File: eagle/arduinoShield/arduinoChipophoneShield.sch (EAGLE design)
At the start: 17 parts

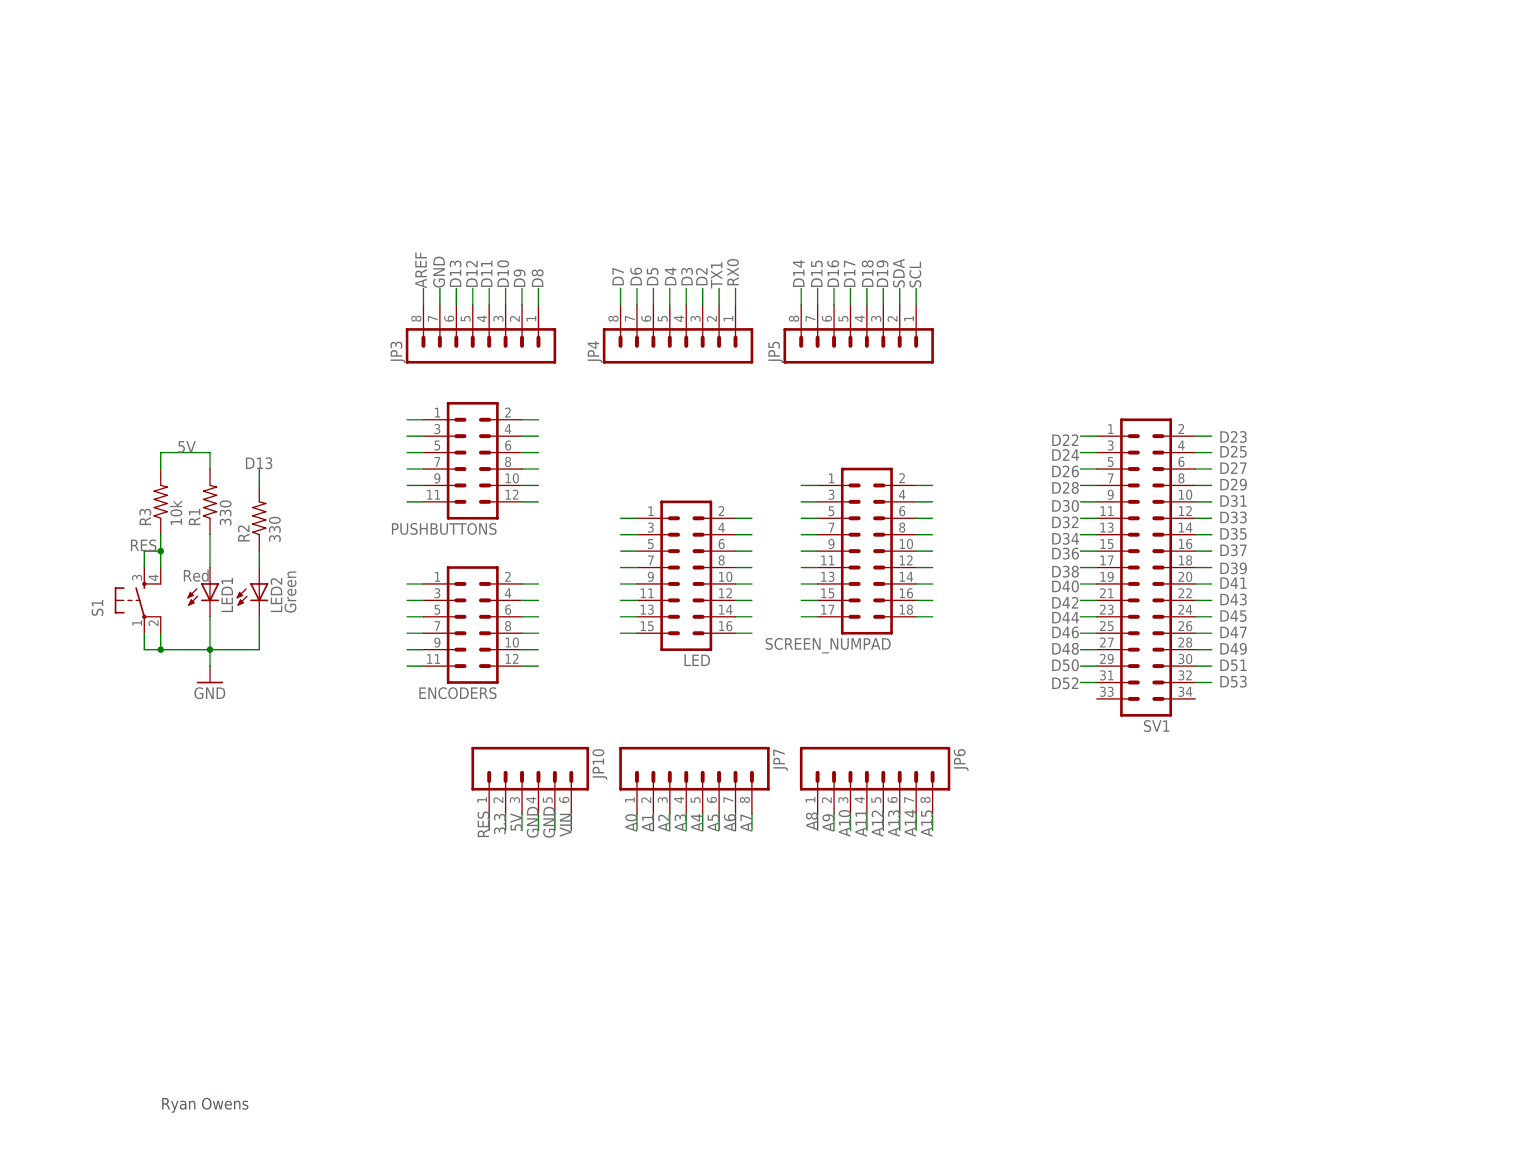
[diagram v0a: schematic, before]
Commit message: Added MIDI I/O, took out status light
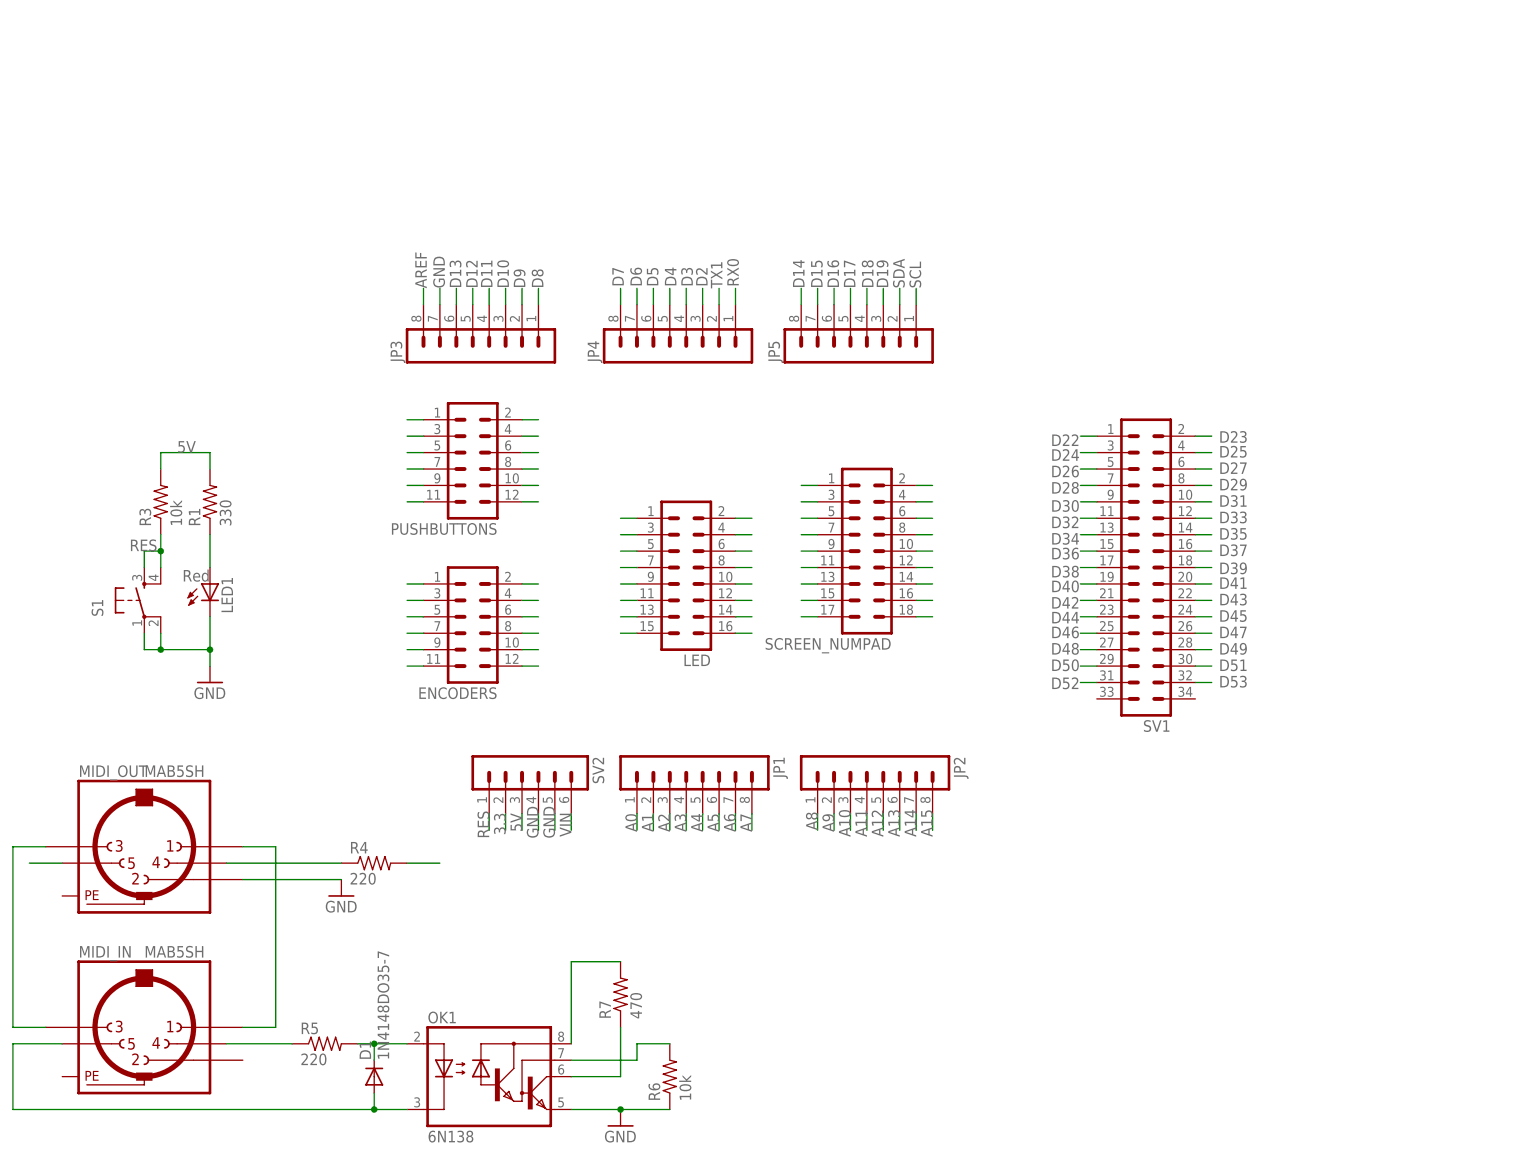
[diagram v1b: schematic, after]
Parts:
- removed JP10: (no value), SparkFun:M06LOCK
- removed JP6, JP7: (no value), SparkFun:M08LOCK
- removed LED2: Green, SparkFun:LED5MM
- removed R2: 330, SparkFun:RESISTORPTH1
- added D1: 1N4148DO35-7, diode:1N4148DO35-7
- added JP1, JP2: (no value), con-lstb:MA08-1
- added MIDI_IN, MIDI_OUT: MAB5SH, con-hirschmann:MAB5SH
- added OK1: 6N138, optocoupler:6N138
- added R4, R5: 220, rcl:R-US_0204/7
- added R6: 10k, rcl:R-US_0204/7
- added R7: 470, rcl:R-US_0204/7
- added SV2: (no value), con-lstb:MA06-1
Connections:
- removed net N$127: LED2.A, R2.1
- new net N$1: MIDI_IN.3, MIDI_OUT.3
- new net N$2: MIDI_IN.1, MIDI_OUT.1
- new net N$3: MIDI_OUT.4, R4.1
- new net N$5: D1.C, OK1.A, R5.2
- new net N$6: MIDI_IN.4, R5.1
- new net N$7: D1.A, MIDI_IN.5, OK1.C
- new net N$8: OK1.VB, R6.2
- net 3.3: now also SV2.2; no longer JP10.2
- net 5V: now also OK1.VCC, R4.2, R7.2, SV2.3; no longer JP10.3
- net A0: now also JP1.1; no longer JP7.1
- net A1: now also JP1.2; no longer JP7.2
- net A10: now also JP2.3; no longer JP6.3
- net A11: now also JP2.4; no longer JP6.4
- net A12: now also JP2.5; no longer JP6.5
- net A13: now also JP2.6; no longer JP6.6
- net A14: now also JP2.7; no longer JP6.7
- net A15: now also JP2.8; no longer JP6.8
- net A2: now also JP1.3; no longer JP7.3
- net A3: now also JP1.4; no longer JP7.4
- net A4: now also JP1.5; no longer JP7.5
- net A5: now also JP1.6; no longer JP7.6
- net A6: now also JP1.7; no longer JP7.7
- net A7: now also JP1.8; no longer JP7.8
- net A8: now also JP2.1; no longer JP6.1
- net A9: now also JP2.2; no longer JP6.2
- net D13: no longer R2.2
- net GND: now also MIDI_OUT.2, OK1.GND, R6.1, SV2.4, SV2.5; no longer JP10.4, JP10.5, LED2.C
- net RES: now also SV2.1; no longer JP10.1
- net RX0: now also OK1.VO, R7.1
- net TX1: now also MIDI_OUT.5
- net VIN: now also SV2.6; no longer JP10.6
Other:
- note removed: "Ryan Owens"

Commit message: Added ground/power plane as well as 5V DIN forwarding switches on Arduino Board
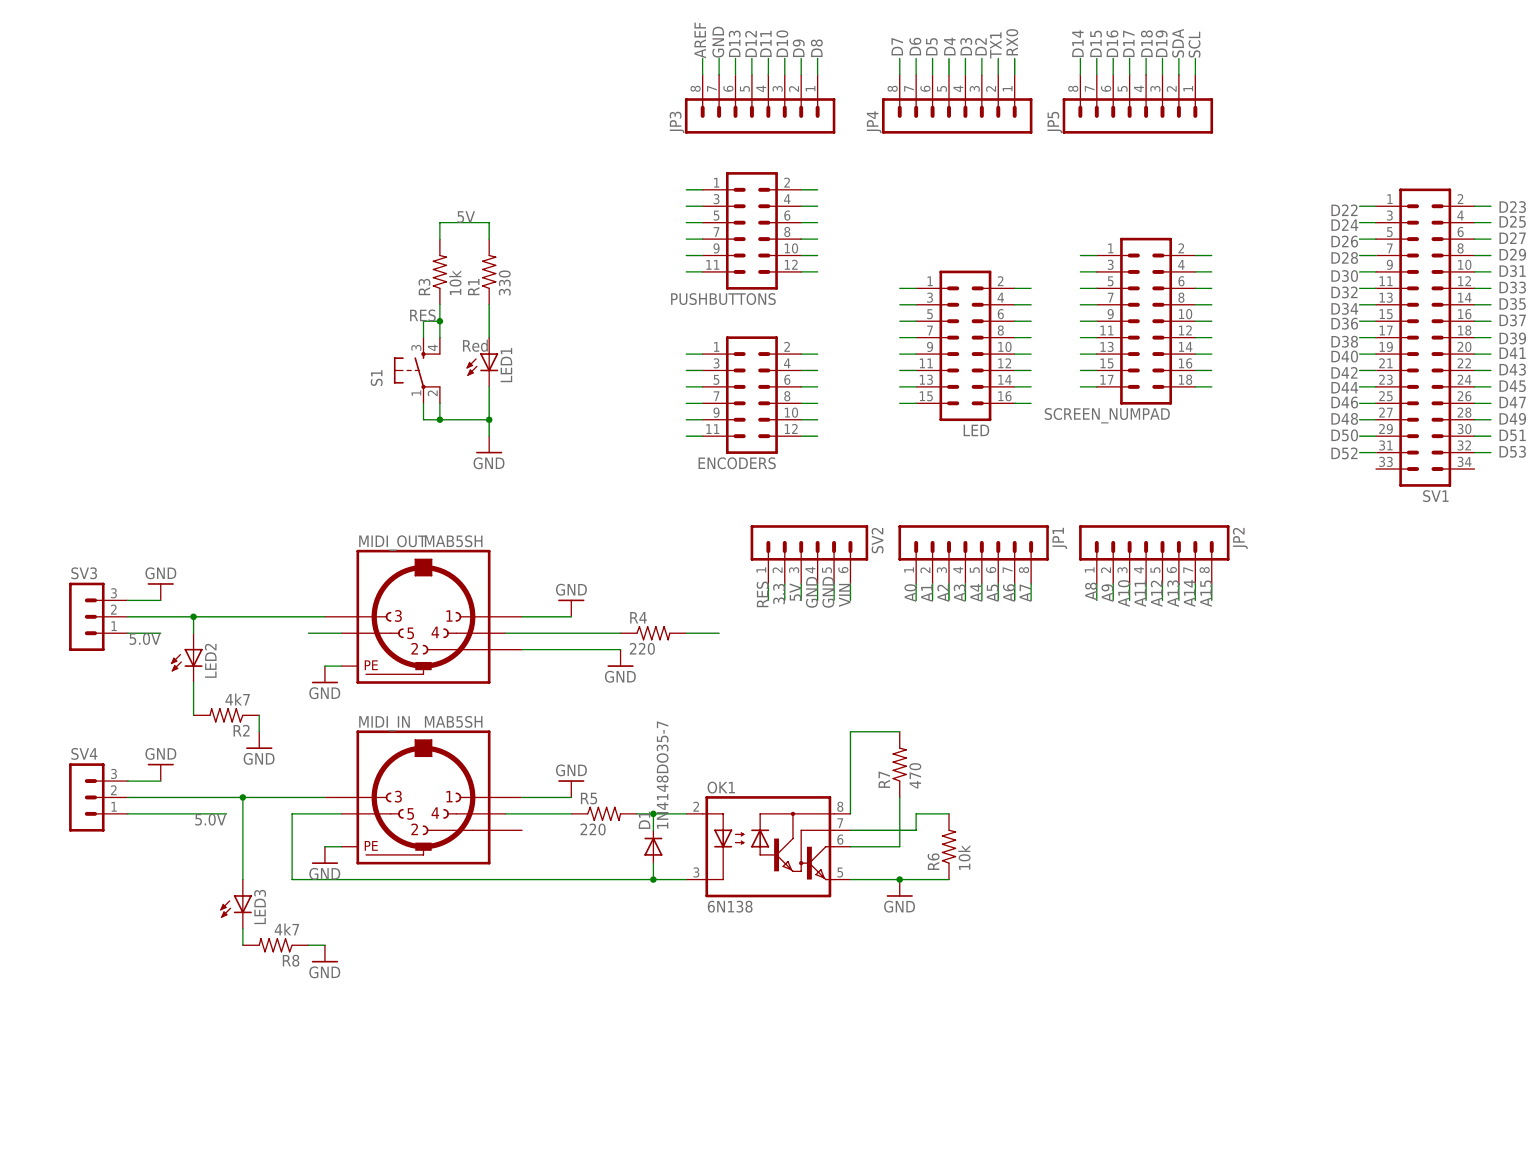
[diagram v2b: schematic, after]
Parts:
- added LED2, LED3: (no value), led:LEDLSU260
- added R2, R8: 4k7, resistor:R-US_0204/7
- added SV3, SV4: (no value), con-lstb:MA03-1
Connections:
- new net N$13: LED3.C, R8.2
- new net N$4: LED2.C, R2.2
- net 5V: now also SV3.1, SV4.1
- net GND: now also MIDI_IN.1, MIDI_IN.PE, MIDI_OUT.1, MIDI_OUT.PE, R2.1, R8.1, SV3.3, SV4.3
- net N$1: now also LED3.A, SV4.2; no longer MIDI_OUT.3
- net N$2: now also LED2.A, MIDI_OUT.3, SV3.2; no longer MIDI_IN.1, MIDI_OUT.1
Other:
- moved on the sheet: D1, ENCODERS, JP1, JP2, JP3, JP4, JP5, LED, LED1, MIDI_IN, MIDI_OUT, OK1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

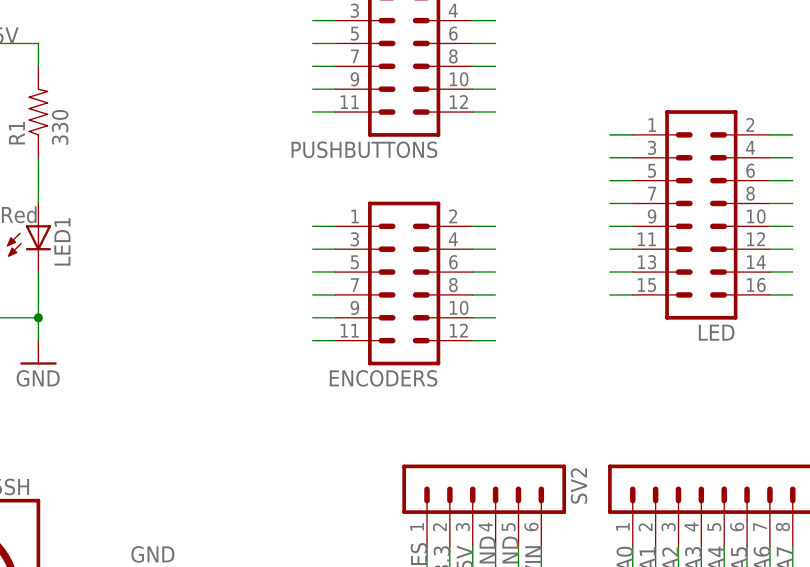
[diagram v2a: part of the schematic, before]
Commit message: Ripped up unnecessary traces due to ground/power planes. Also switched encoder common to ground to use internal pullup resistors
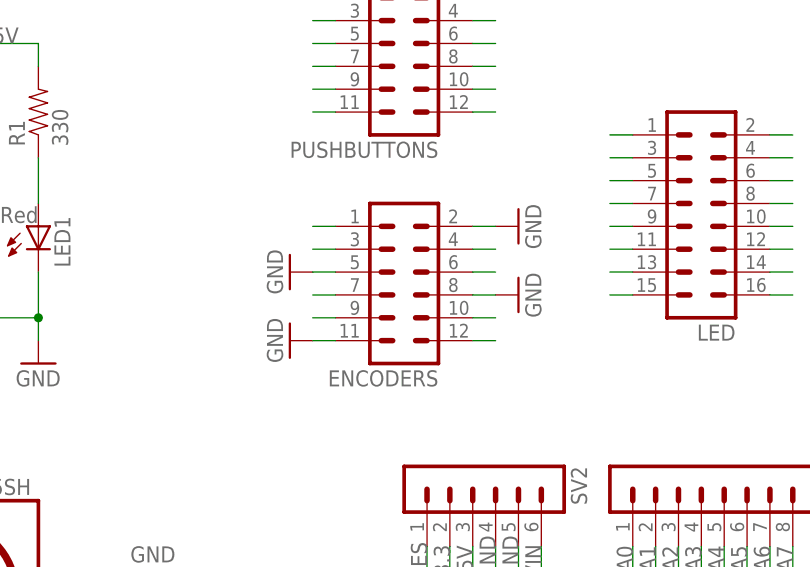
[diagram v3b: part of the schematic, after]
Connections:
- net 5V: no longer ENCODERS.11, ENCODERS.2, ENCODERS.5, ENCODERS.8
- net GND: now also ENCODERS.11, ENCODERS.2, ENCODERS.5, ENCODERS.8
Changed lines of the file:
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@@
 <part name="R8" library="resistor" deviceset="R-US_" device="0204/7" value="4k7"/>
 <part name="GND12" library="supply1" deviceset="GND" device=""/>
+<part name="GND9" library="SparkFun" deviceset="GND" device=""/>
+<part name="GND13" library="SparkFun" deviceset="GND" device=""/>
+<part name="GND14" library="SparkFun" deviceset="GND" device=""/>
+<part name="GND15" library="SparkFun" deviceset="GND" device=""/>
 </parts>
 <sheets>
@@
 <instance part="R8" gate="G$1" x="48.26" y="35.56" rot="R180"/>
 <instance part="GND12" gate="1" x="55.88" y="33.02"/>
+<instance part="GND9" gate="1" x="134.62" y="127" rot="R90"/>
+<instance part="GND13" gate="1" x="134.62" y="119.38" rot="R90"/>
+<instance part="GND14" gate="1" x="109.22" y="121.92" rot="R270"/>
+<instance part="GND15" gate="1" x="109.22" y="114.3" rot="R270"/>
 </instances>
 <busses>
@@
 <pinref part="R3" gate="G$1" pin="2"/>
 <pinref part="R1" gate="G$1" pin="2"/>
-</segment>
-<segment>
-<wire x1="132.08" y1="127" x2="129.54" y2="127" width="0.1524" layer="91"/>
-<pinref part="ENCODERS" gate="1" pin="2"/>
-</segment>
-<segment>
-<wire x1="114.3" y1="121.92" x2="111.76" y2="121.92" width="0.1524" layer="91"/>
-<pinref part="ENCODERS" gate="1" pin="5"/>
-</segment>
-<segment>
-<wire x1="132.08" y1="119.38" x2="129.54" y2="119.38" width="0.1524" layer="91"/>
-<pinref part="ENCODERS" gate="1" pin="8"/>
-</segment>
-<segment>
-<wire x1="114.3" y1="114.3" x2="111.76" y2="114.3" width="0.1524" layer="91"/>
-<pinref part="ENCODERS" gate="1" pin="11"/>
 </segment>
 <segment>
@@
 <wire x1="55.88" y1="50.8" x2="58.42" y2="50.8" width="0.1524" layer="91"/>
 </segment>
-</net>
+<segment>
+<wire x1="132.08" y1="127" x2="129.54" y2="127" width="0.1524" layer="91"/>
+<pinref part="ENCODERS" gate="1" pin="2"/>
+<pinref part="GND9" gate="1" pin="GND"/>
+</segment>
+<segment>
+<wire x1="132.08" y1="119.38" x2="129.54" y2="119.38" width="0.1524" layer="91"/>
+<pinref part="ENCODERS" gate="1" pin="8"/>
+<pinref part="GND13" gate="1" pin="GND"/>
+</segment>
+<segment>
+<wire x1="114.3" y1="121.92" x2="111.76" y2="121.92" width="0.1524" layer="91"/>
+<pinref part="ENCODERS" gate="1" pin="5"/>
+<pinref part="GND14" gate="1" pin="GND"/>
+</segment>
+<segment>
+<wire x1="114.3" y1="114.3" x2="111.76" y2="114.3" width="0.1524" layer="91"/>
+<pinref part="ENCODERS" gate="1" pin="11"/>
+<pinref part="GND15" gate="1" pin="GND"/>
+</segment>
+</net>

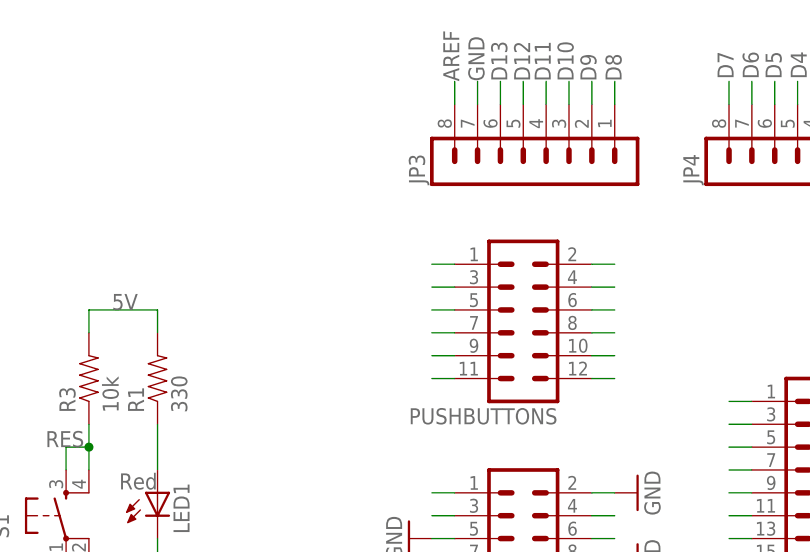
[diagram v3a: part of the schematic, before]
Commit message: Updated so switches can also use internal pullup resistors
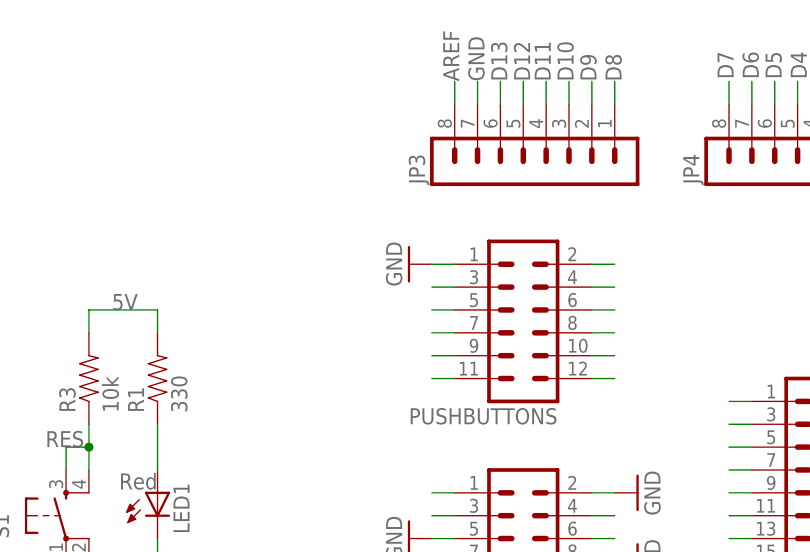
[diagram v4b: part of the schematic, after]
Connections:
- net 5V: no longer PUSHBUTTONS.1
- net GND: now also PUSHBUTTONS.1
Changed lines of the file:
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@@
 <part name="GND14" library="SparkFun" deviceset="GND" device=""/>
 <part name="GND15" library="SparkFun" deviceset="GND" device=""/>
+<part name="GND16" library="SparkFun" deviceset="GND" device=""/>
 </parts>
 <sheets>
@@
 <instance part="GND14" gate="1" x="109.22" y="121.92" rot="R270"/>
 <instance part="GND15" gate="1" x="109.22" y="114.3" rot="R270"/>
+<instance part="GND16" gate="1" x="109.22" y="152.4" rot="R270"/>
 </instances>
 <busses>
@@
 <pinref part="R3" gate="G$1" pin="2"/>
 <pinref part="R1" gate="G$1" pin="2"/>
-</segment>
-<segment>
-<wire x1="114.3" y1="152.4" x2="111.76" y2="152.4" width="0.1524" layer="91"/>
-<pinref part="PUSHBUTTONS" gate="1" pin="1"/>
 </segment>
 <segment>
@@
 <pinref part="GND15" gate="1" pin="GND"/>
 </segment>
-</net>
+<segment>
+<wire x1="114.3" y1="152.4" x2="111.76" y2="152.4" width="0.1524" layer="91"/>
+<pinref part="PUSHBUTTONS" gate="1" pin="1"/>
+<pinref part="GND16" gate="1" pin="GND"/>
+</segment>
+</net>
